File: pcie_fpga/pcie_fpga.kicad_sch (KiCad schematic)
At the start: 4 parts, among them J2 PCIexpress_x8, U2 XCAU10P-1FFVB676I, X1 ECS-2520MVQ-1000-BN-TR

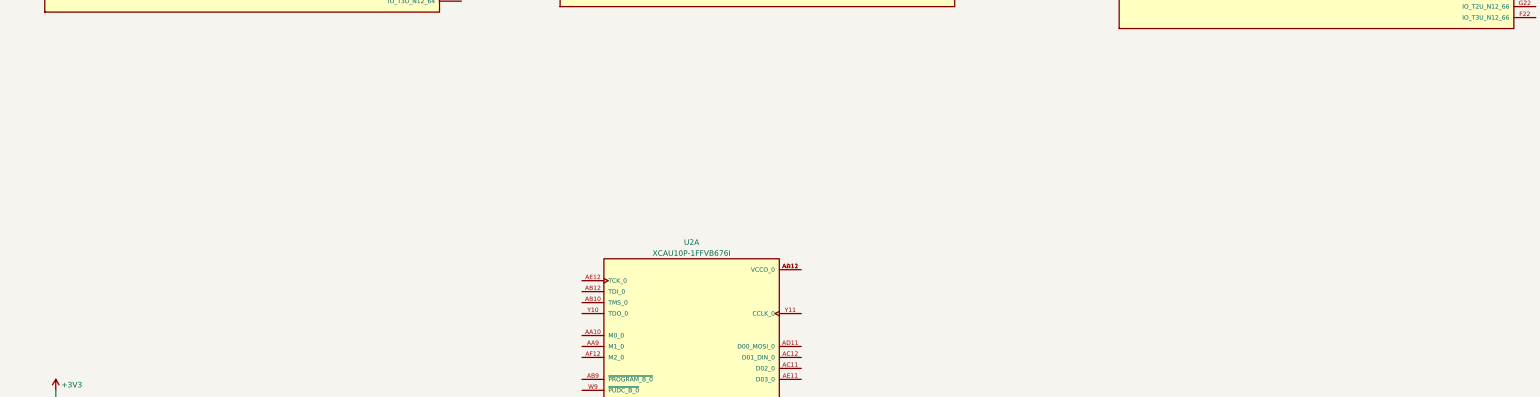
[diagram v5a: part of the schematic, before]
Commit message: added PMOD and JTAG connectors
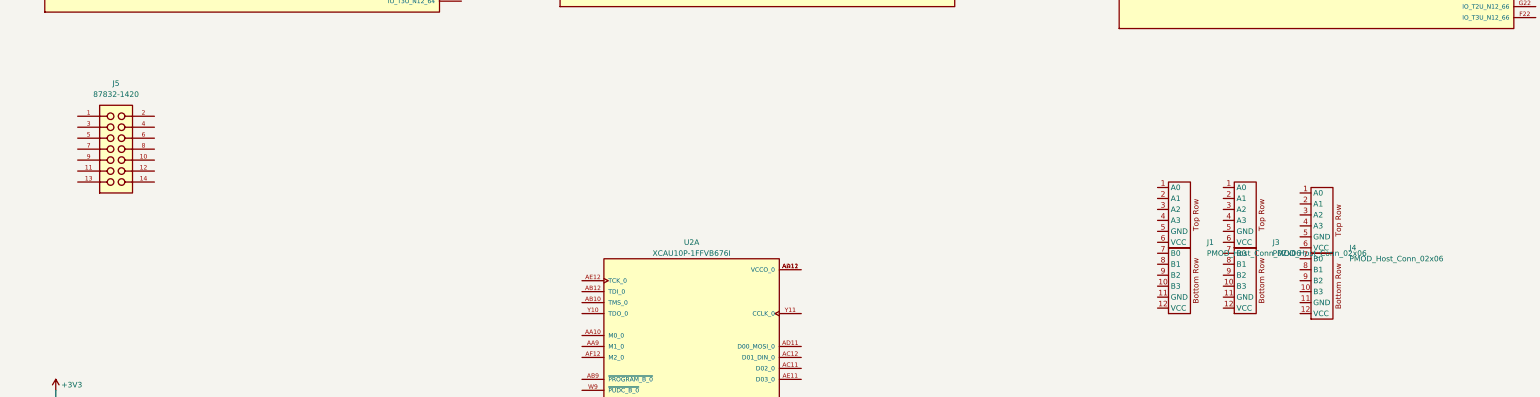
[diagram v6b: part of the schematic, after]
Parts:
- added J1, J3, J4: PMOD_Host_Conn_02x06, pedrolib:PMOD_PinSocket_2x06_P2.54mm_Horizontal, symbol pedrolib:PMOD_Host_Conn_02x06
- added J5: 87832-1420, pedrolib:MOLEX_87832-1420, symbol pedrolib:87832-1420
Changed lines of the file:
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@@
     (pin "1")
   )
+  (symbol (lib_id "pedrolib:87832-1420") (at 52.07 171.45 0) (unit 1)
+    (in_bom yes) (on_board yes) (fields_autoplaced)
+    (property "Reference" "J5" (id 0) (at 50.8 156.21 0))
+    (property "Value" "87832-1420" (id 1) (at 50.8 158.75 0))
+    (property "Footprint" "pedrolib:MOLEX_87832-1420" (id 2) (at 50.8 185.42 0)
+      (effects (font (size 1.27 1.27)) (justify bottom) hide)
+    )
+    (property "Datasheet" "" (id 3) (at 52.07 171.45 0)
+      (effects (font (size 1.27 1.27)) hide)
+    )
+    (property "MANUFACTURER" "MOLEX" (id 4) (at 52.07 171.45 0)
+      (effects (font (size 1.27 1.27)) (justify bottom) hide)
+    )
+    (pin "1")
+    (pin "10")
+    (pin "11")
+    (pin "12")
+    (pin "13")
+    (pin "14")
+    (pin "2")
+    (pin "3")
+    (pin "4")
+    (pin "5")
+    (pin "6")
+    (pin "7")
+    (pin "8")
+    (pin "9")
+  )
   (symbol (lib_id "power:+3.3VA") (at 69.85 303.53 90) (unit 1)
     (in_bom yes) (on_board yes)
@@
     (pin "K7")
   )
+  (symbol (lib_id "pedrolib:PMOD_Host_Conn_02x06") (at 312.42 194.31 0) (unit 1)
+    (in_bom yes) (on_board yes) (fields_autoplaced)
+    (property "Reference" "J3" (id 0) (at 318.77 193.0399 0)
+      (effects (font (size 1.27 1.27)) (justify left))
+    )
+    (property "Value" "PMOD_Host_Conn_02x06" (id 1) (at 318.77 195.5799 0)
+      (effects (font (size 1.27 1.27)) (justify left))
+    )
+    (property "Footprint" "pedrolib:PMOD_PinSocket_2x06_P2.54mm_Horizontal" (id 2) (at 289.56 198.12 0)
+      (effects (font (size 1.27 1.27)) hide)
+    )
+    (property "Datasheet" "" (id 3) (at 289.56 198.12 0)
+      (effects (font (size 1.27 1.27)) hide)
+    )
+    (pin "1")
+    (pin "10")
+    (pin "11")
+    (pin "12")
+    (pin "2")
+    (pin "3")
+    (pin "4")
+    (pin "5")
+    (pin "6")
+    (pin "7")
+    (pin "8")
+    (pin "9")
+  )
   (symbol (lib_id "power:+3V3") (at 36.83 227.33 0) (unit 1)
     (in_bom yes) (on_board yes)
@@
     (pin "1")
   )
+  (symbol (lib_id "pedrolib:PMOD_Host_Conn_02x06") (at 330.2 195.58 0) (unit 1)
+    (in_bom yes) (on_board yes) (fields_autoplaced)
+    (property "Reference" "J4" (id 0) (at 336.55 194.3099 0)
+      (effects (font (size 1.27 1.27)) (justify left))
+    )
+    (property "Value" "PMOD_Host_Conn_02x06" (id 1) (at 336.55 196.8499 0)
+      (effects (font (size 1.27 1.27)) (justify left))
+    )
+    (property "Footprint" "pedrolib:PMOD_PinSocket_2x06_P2.54mm_Horizontal" (id 2) (at 307.34 199.39 0)
+      (effects (font (size 1.27 1.27)) hide)
+    )
+    (property "Datasheet" "" (id 3) (at 307.34 199.39 0)
+      (effects (font (size 1.27 1.27)) hide)
+    )
+    (pin "1")
+    (pin "10")
+    (pin "11")
+    (pin "12")
+    (pin "2")
+    (pin "3")
+    (pin "4")
+    (pin "5")
+    (pin "6")
+    (pin "7")
+    (pin "8")
+    (pin "9")
+  )
   (symbol (lib_id "pedrolib:XCAU10P-1FFVB676I") (at 481.33 255.27 0) (unit 11)
     (in_bom yes) (on_board yes) (fields_autoplaced)
@@
     (pin "1")
   )
+  (symbol (lib_id "pedrolib:PMOD_Host_Conn_02x06") (at 297.18 194.31 0) (unit 1)
+    (in_bom yes) (on_board yes) (fields_autoplaced)
+    (property "Reference" "J1" (id 0) (at 303.53 193.0399 0)
+      (effects (font (size 1.27 1.27)) (justify left))
+    )
+    (property "Value" "PMOD_Host_Conn_02x06" (id 1) (at 303.53 195.5799 0)
+      (effects (font (size 1.27 1.27)) (justify left))
+    )
+    (property "Footprint" "pedrolib:PMOD_PinSocket_2x06_P2.54mm_Horizontal" (id 2) (at 274.32 198.12 0)
+      (effects (font (size 1.27 1.27)) hide)
+    )
+    (property "Datasheet" "" (id 3) (at 274.32 198.12 0)
+      (effects (font (size 1.27 1.27)) hide)
+    )
+    (pin "1")
+    (pin "10")
+    (pin "11")
+    (pin "12")
+    (pin "2")
+    (pin "3")
+    (pin "4")
+    (pin "5")
+    (pin "6")
+    (pin "7")
+    (pin "8")
+    (pin "9")
+  )
   (symbol (lib_id "power:GND") (at 107.95 414.02 0) (mirror y) (unit 1)
     (in_bom yes) (on_board yes)
@@
       (reference "#PWR012") (unit 1) (value "GND") (footprint "")
     )
+    (path "/ef38905b-9d4a-46a8-b343-cbaab6de45f2"
+      (reference "J1") (unit 1) (value "PMOD_Host_Conn_02x06") (footprint "pedrolib:PMOD_PinSocket_2x06_P2.54mm_Horizontal")
+    )
     (path "/5fb904a1-b41e-4963-94a4-b4c48084d9ef"
       (reference "J2") (unit 1) (value "PCIexpress_x8") (footprint "pedrolib:PCIexpress_x8")
     )
+    (path "/54da5a8e-314f-4a95-addb-a14995a85294"
+      (reference "J3") (unit 1) (value "PMOD_Host_Conn_02x06") (footprint "pedrolib:PMOD_PinSocket_2x06_P2.54mm_Horizontal")
+    )
+    (path "/92061954-5e94-41c4-a3fd-0a59bf03c09e"
+      (reference "J4") (unit 1) (value "PMOD_Host_Conn_02x06") (footprint "pedrolib:PMOD_PinSocket_2x06_P2.54mm_Horizontal")
+    )
+    (path "/43c552fe-2192-4bef-9075-3f0c7618ae61"
+      (reference "J5") (unit 1) (value "87832-1420") (footprint "pedrolib:MOLEX_87832-1420")
+    )
     (path "/80450a8a-de64-4455-a65d-feef0126ac56"

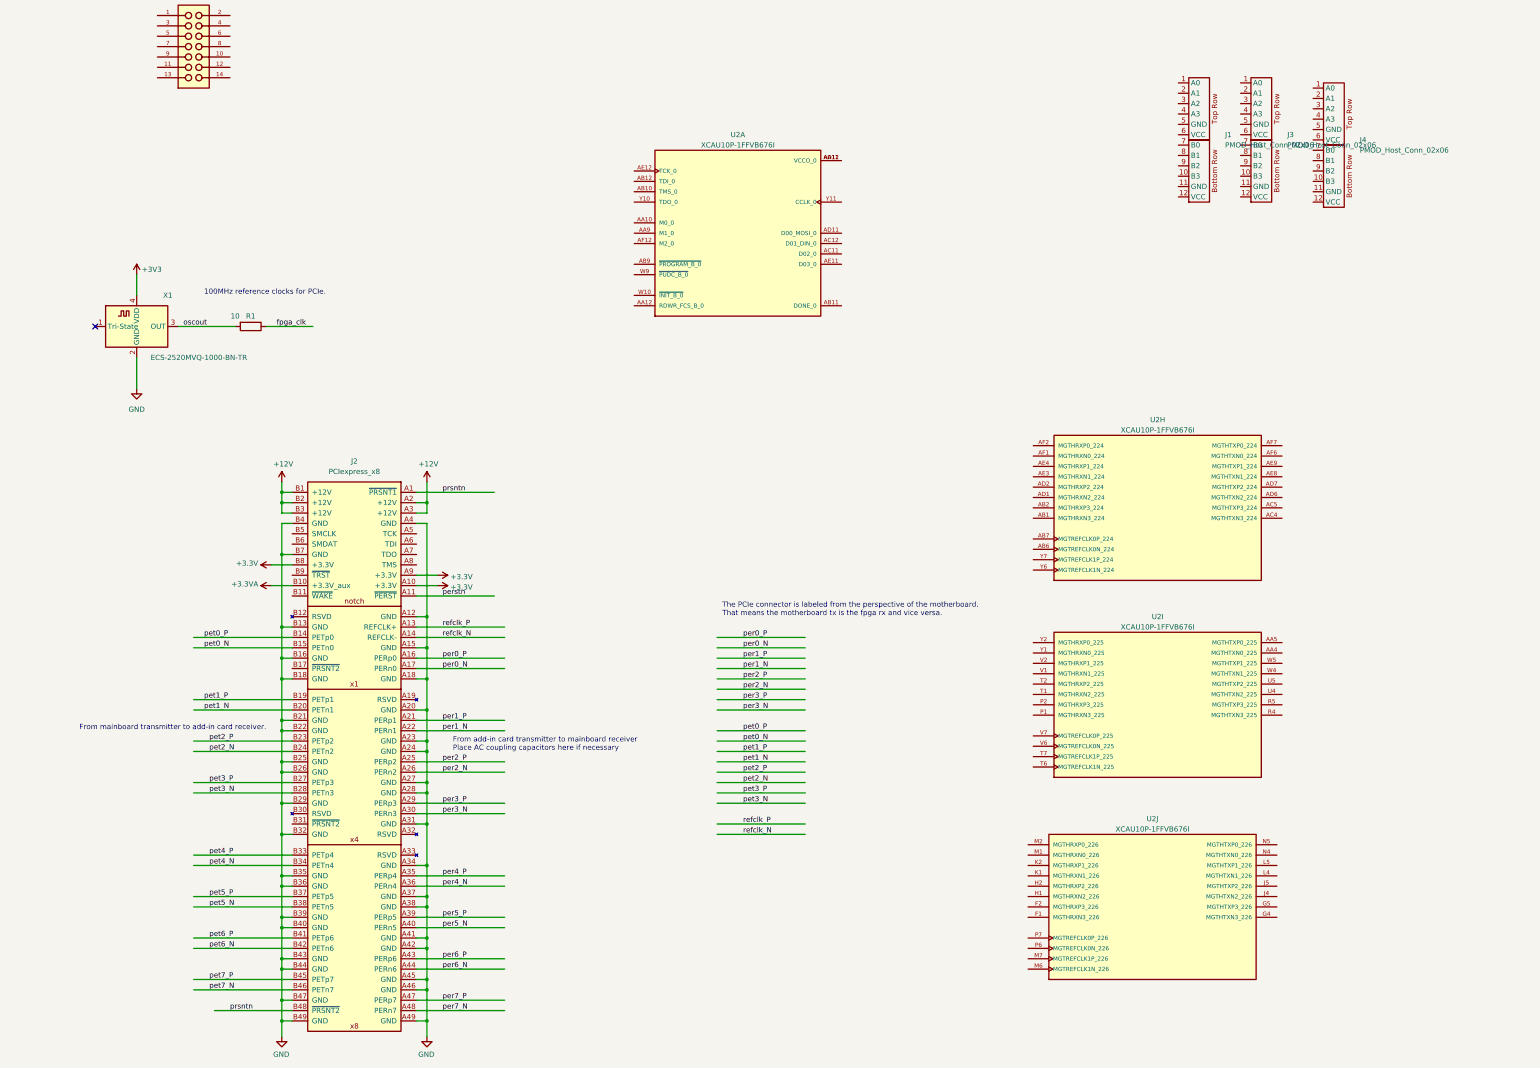
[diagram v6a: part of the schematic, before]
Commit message: wired pcie links with ac coupling caps
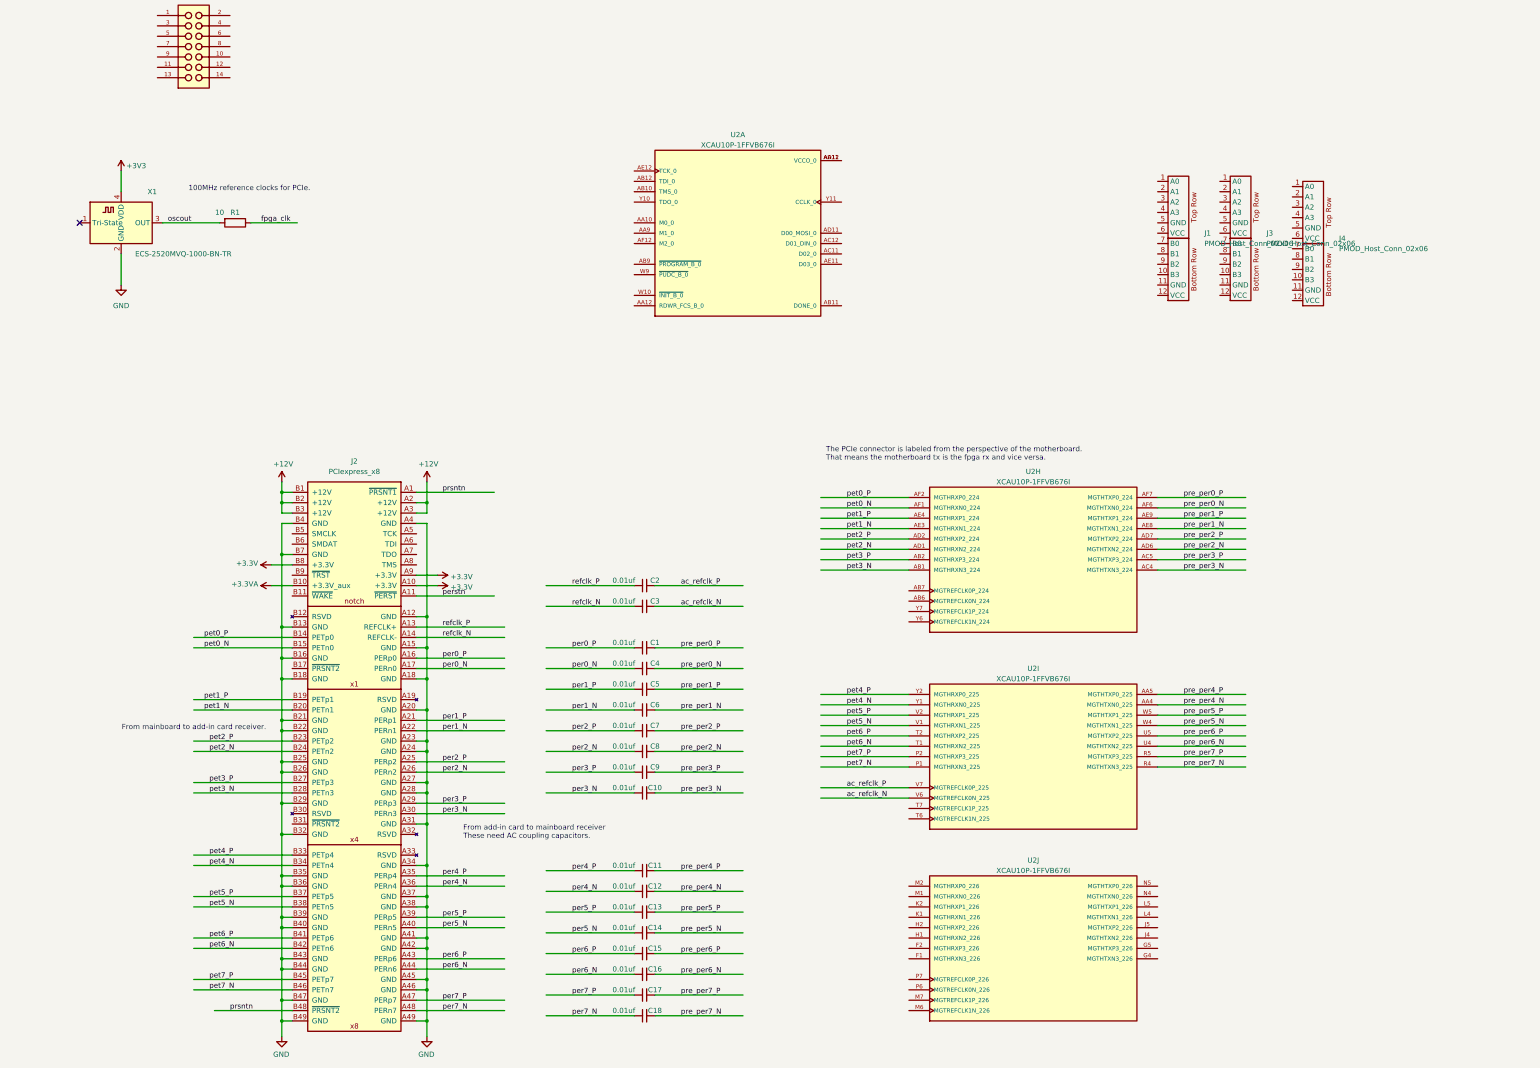
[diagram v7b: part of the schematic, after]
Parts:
- added C1, C10, C11, C12, C13, C14, C15, C16, C17, C18, C2, C3, C4, C5, C6, C7, C8, C9: 0.01uf, Capacitor_SMD:C_0402_1005Metric, symbol Device:C_Small
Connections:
- net per0_N: now also C4.1
- net per0_P: now also C1.1
- net per1_N: now also C6.1
- net per1_P: now also C5.1
- net per2_N: now also C8.1
- net per2_P: now also C7.1
- net per3_N: now also C10.1
- net per3_P: now also C9.1
- net per4_N: now also C12.1
- net per4_P: now also C11.1
- net per5_N: now also C14.1
- net per5_P: now also C13.1
- net per6_N: now also C16.1
- net per6_P: now also C15.1
- net per7_N: now also C18.1
- net per7_P: now also C17.1
- net pet0_N: now also U2.AF1 (MGTHRXN0_224)
- net pet0_P: now also U2.AF2 (MGTHRXP0_224)
- net pet1_N: now also U2.AE3 (MGTHRXN1_224)
- net pet1_P: now also U2.AE4 (MGTHRXP1_224)
- net pet2_N: now also U2.AD1 (MGTHRXN2_224)
- net pet2_P: now also U2.AD2 (MGTHRXP2_224)
- net pet3_N: now also U2.AB1 (MGTHRXN3_224)
- net pet3_P: now also U2.AB2 (MGTHRXP3_224)
- net pet4_N: now also U2.Y1 (MGTHRXN0_225)
- net pet4_P: now also U2.Y2 (MGTHRXP0_225)
- net pet5_N: now also U2.V1 (MGTHRXN1_225)
- net pet5_P: now also U2.V2 (MGTHRXP1_225)
- net pet6_N: now also U2.T1 (MGTHRXN2_225)
- net pet6_P: now also U2.T2 (MGTHRXP2_225)
- net pet7_N: now also U2.P1 (MGTHRXN3_225)
- net pet7_P: now also U2.P2 (MGTHRXP3_225)
- net refclk_N: now also C3.1
- net refclk_P: now also C2.1
- net pre_per3_N: now reaches U2.AC4 (MGTHTXN3_224)
- net pre_per3_N: now also C10.2
- net pre_per3_P: now reaches U2.AC5 (MGTHTXP3_224)
- net pre_per3_P: now also C9.2
- net pre_per2_N: now reaches U2.AD6 (MGTHTXN2_224)
- net pre_per2_N: now also C8.2
- net pre_per2_P: now reaches U2.AD7 (MGTHTXP2_224)
- net pre_per2_P: now also C7.2
- net pre_per1_N: now reaches U2.AE8 (MGTHTXN1_224)
- net pre_per1_N: now also C6.2
- net pre_per1_P: now reaches U2.AE9 (MGTHTXP1_224)
- net pre_per1_P: now also C5.2
- net pre_per0_N: now reaches U2.AF6 (MGTHTXN0_224)
- net pre_per0_N: now also C4.2
- net pre_per0_P: now reaches U2.AF7 (MGTHTXP0_224)
- net pre_per0_P: now also C1.2
- net pre_per4_N: now reaches U2.AA4 (MGTHTXN0_225)
- net pre_per4_N: now also C12.2
- net pre_per4_P: now reaches U2.AA5 (MGTHTXP0_225)
- net pre_per4_P: now also C11.2
- net pre_per7_N: now reaches U2.R4 (MGTHTXN3_225)
- net pre_per7_N: now also C18.2
- net pre_per7_P: now reaches U2.R5 (MGTHTXP3_225)
- net pre_per7_P: now also C17.2
- net pre_per6_N: now reaches U2.U4 (MGTHTXN2_225)
- net pre_per6_N: now also C16.2
- net pre_per6_P: now reaches U2.U5 (MGTHTXP2_225)
- net pre_per6_P: now also C15.2
- net ac_refclk_N: now reaches U2.V6 (MGTREFCLK0N_225)
- net ac_refclk_N: now also C3.2
- net ac_refclk_P: now reaches U2.V7 (MGTREFCLK0P_225)
- net ac_refclk_P: now also C2.2
- net pre_per5_N: now reaches U2.W4 (MGTHTXN1_225)
- net pre_per5_N: now also C14.2
- net pre_per5_P: now reaches U2.W5 (MGTHTXP1_225)
- net pre_per5_P: now also C13.2
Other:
- note added: "From add-in card to mainboard receiver These need AC coupling capacitors."
- note added: "From mainboard to add-in card receiver."
- note removed: "From add-in card transmitter to mainboard receiver Place AC coupling capacitors here if necessary"
- note removed: "From mainboard transmitter to add-in card receiver."
- moved on the sheet: J1, J3, J4, R1, U2H, U2I, U2J, X1
